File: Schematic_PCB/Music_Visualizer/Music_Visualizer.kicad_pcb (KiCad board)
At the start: 2 copper layers, 115 parts, among them J1 AudioJack2_Ground, SW1 SW_SPDT, U1 LM324, U2 LM324, U3 LM324, U4 LM324, U5 LM324, U6 LM324

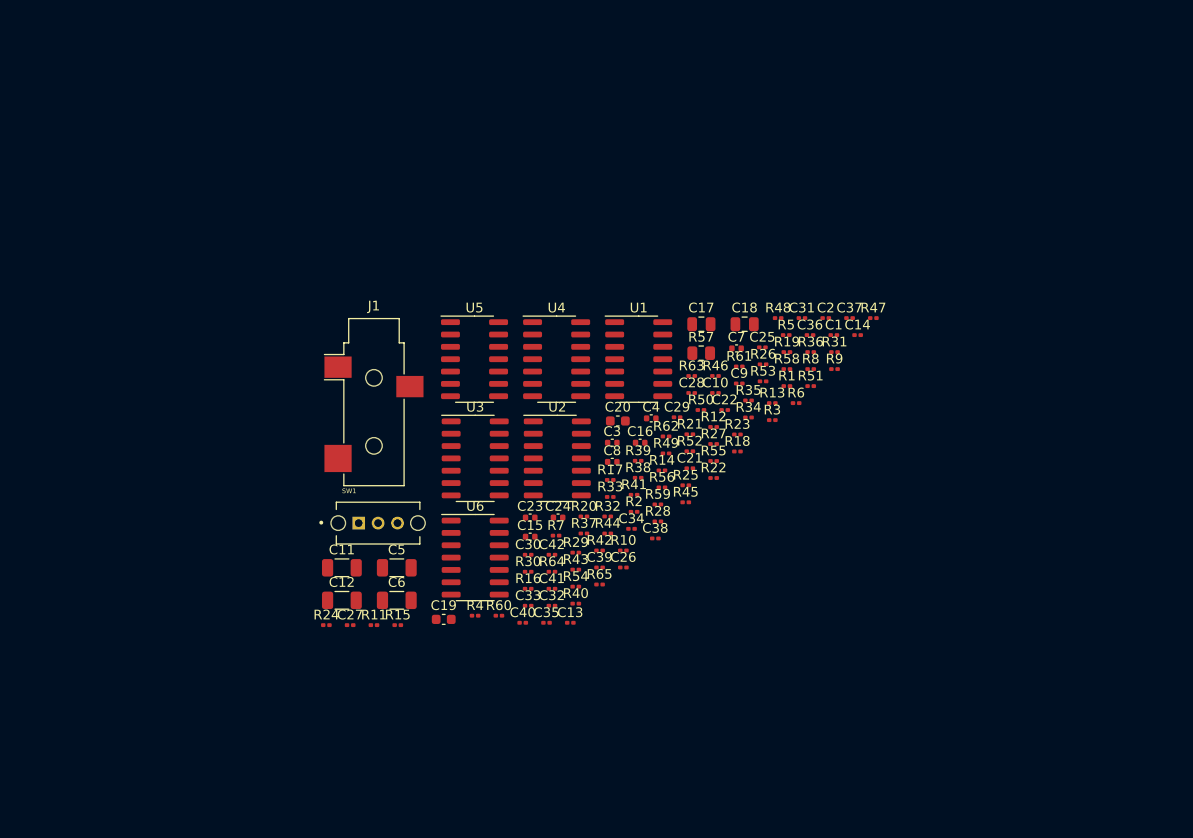
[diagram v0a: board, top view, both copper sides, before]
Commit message: Used Global labels
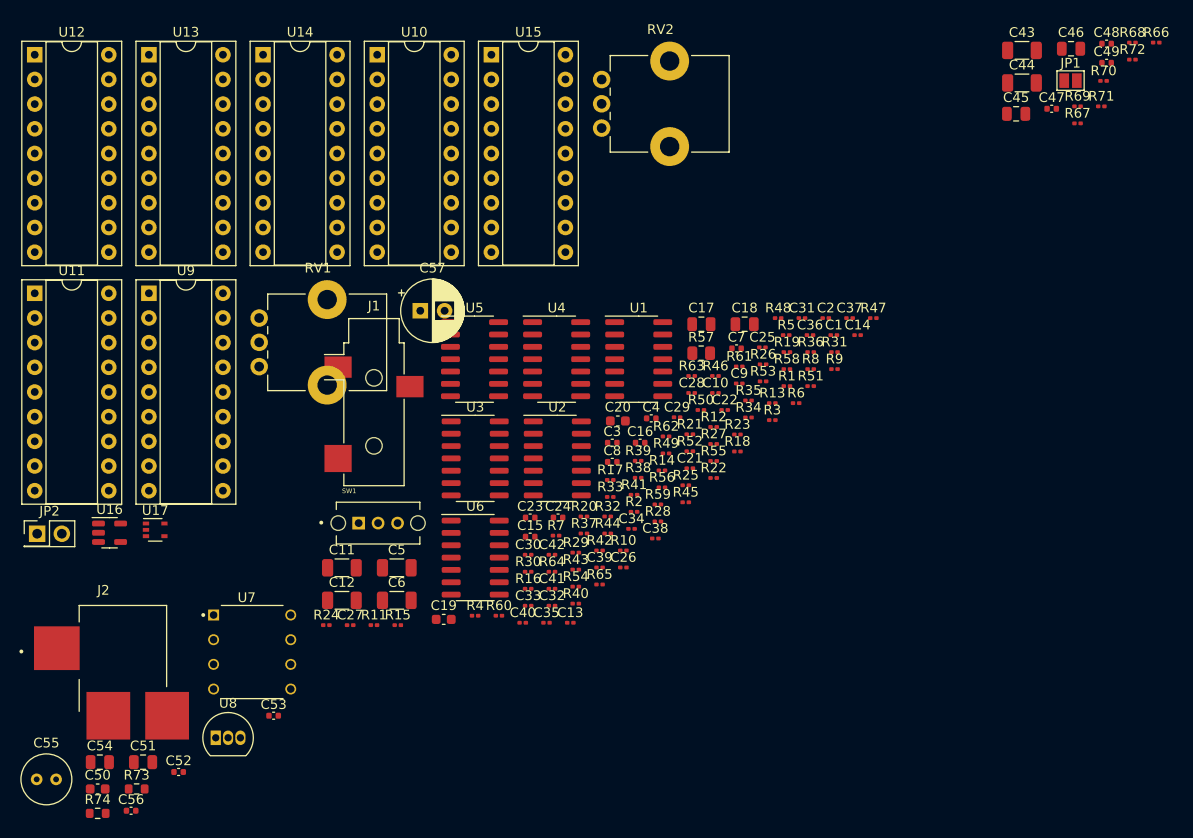
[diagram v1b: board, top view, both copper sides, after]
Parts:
- added C43: 100u, Capacitor_SMD:C_1206_3216Metric, F.Cu at (103.2, 1.18)
- added C44: 100u, Capacitor_SMD:C_1206_3216Metric, F.Cu at (103.2, 4.53)
- added C45: 10u, Capacitor_SMD:C_0805_2012Metric, F.Cu at (102.6, 7.71)
- added C46: 10u, Capacitor_SMD:C_0805_2012Metric, F.Cu at (108.2, 1.00)
- added C47: 1u, Capacitor_SMD:C_0402_1005Metric, F.Cu at (106.2, 7.18)
- added C48: 1u, Capacitor_SMD:C_0402_1005Metric, F.Cu at (111.9, 0.48)
- added C49: 1u, Capacitor_SMD:C_0402_1005Metric, F.Cu at (111.9, 2.46)
- added C50: 0.33uF, Capacitor_SMD:C_0603_1608Metric, F.Cu at (8.05, 77.2)
- added C51: 0.1uF, Capacitor_SMD:C_0805_2012Metric, F.Cu at (12.7, 74.4)
- added C52: 1u, Capacitor_SMD:C_0402_1005Metric, F.Cu at (16.4, 75.4)
- added C53: 1u, Capacitor_SMD:C_0402_1005Metric, F.Cu at (26.2, 69.7)
- added C54: 10u, Capacitor_SMD:C_0805_2012Metric, F.Cu at (8.28, 74.4)
- added C55: 100u, Capacitor_THT:C_Radial_D5.0mm_H5.0mm_P2.00mm, F.Cu at (1.77, 76.2)
- added C56: 0.002u, Capacitor_SMD:C_0402_1005Metric, F.Cu at (11.5, 79.4)
- added C57: 220u, Capacitor_THT:CP_Radial_D6.3mm_P2.50mm, F.Cu at (41.3, 28.0)
- added J2: PJ-070BH-SMT-TR, DC_Power_Jack_PJ_070BH_SMT_TR:CUI_PJ-PJ-070BH-SMT-TR, F.Cu at (10.7, 63.8)
- added JP1: SolderJumper_2_Open, Jumper:SolderJumper-2_P1.3mm_Open_Pad1.0x1.5mm, F.Cu at (108.2, 4.29)
- added JP2: Jumper_2_Open, Connector_PinHeader_2.54mm:PinHeader_2x01_P2.54mm_Vertical, F.Cu at (1.82, 50.9)
- added R66: 1k, Resistor_SMD:R_0201_0603Metric, F.Cu at (117.0, 0.38)
- added R67: 1k, Resistor_SMD:R_0201_0603Metric, F.Cu at (108.9, 8.69)
- added R68: 1k, Resistor_SMD:R_0201_0603Metric, F.Cu at (114.6, 0.38)
- added R69: 1k, Resistor_SMD:R_0201_0603Metric, F.Cu at (108.9, 6.93)
- added R70: 1k, Resistor_SMD:R_0201_0603Metric, F.Cu at (111.6, 4.32)
- added R71: 1k, Resistor_SMD:R_0201_0603Metric, F.Cu at (111.4, 6.93)
- added R72: 1k, Resistor_SMD:R_0201_0603Metric, F.Cu at (114.6, 2.12)
- added R73: 20k, Resistor_SMD:R_0603_1608Metric, F.Cu at (12.1, 77.2)
- added R74: 102k, Resistor_SMD:R_0603_1608Metric, F.Cu at (8.05, 79.7)
- added RV1: 5k_LED_Brightness_Pot, Potentiometer_THT:Potentiometer_Bourns_PTV09A-1_Single_Vertical, F.Cu at (24.7, 33.7)
- added RV2: 5k_Rhi_Adjuster, Potentiometer_THT:Potentiometer_Bourns_PTV09A-1_Single_Vertical, F.Cu at (59.9, 9.18)
- added U10: LM3915N-1, Package_DIP:DIP-18_W7.62mm_Socket, F.Cu at (36.8, 1.62)
- added U11: LM3915N-1, Package_DIP:DIP-18_W7.62mm_Socket, F.Cu at (1.57, 26.2)
- added U12: LM3915N-1, Package_DIP:DIP-18_W7.62mm_Socket, F.Cu at (1.57, 1.62)
- added U13: LM3915N-1, Package_DIP:DIP-18_W7.62mm_Socket, F.Cu at (13.3, 1.62)
- added U14: LM3915N-1, Package_DIP:DIP-18_W7.62mm_Socket, F.Cu at (25.1, 1.62)
- added U15: LM3915N-1, Package_DIP:DIP-18_W7.62mm_Socket, F.Cu at (48.6, 1.62)
- added U16: NCP161ASN350T1G, Package_TO_SOT_SMD:SOT-23-5, F.Cu at (9.28, 50.8)
- added U17: NCS333ASQ3T2G, Package_TO_SOT_SMD:SOT-353_SC-70-5, F.Cu at (14.0, 50.5)
- added U7: LT1054, LT1054_PDIP_Lin_Reg:DIP794W45P254L959H508Q8, F.Cu at (24.0, 63.1)
- added U8: MC78L05_TO92, Package_TO_SOT_THT:TO-92_Inline, F.Cu at (20.2, 71.9)
- added U9: LM3915N-1, Package_DIP:DIP-18_W7.62mm_Socket, F.Cu at (13.3, 26.2)
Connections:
- J1 pad T: /Vsig -> Net-(J1-PadT)
- R1 pad 1: /Vsig -> Vsig
- R10 pad 1: /Vsig -> Vsig
- R20 pad 1: /Vsig -> Vsig
- R29 pad 1: /Vsig -> Vsig
- R39 pad 1: /Vsig -> Vsig
- R48 pad 1: /Vsig -> Vsig
- R57 pad 1: /Vsig -> Vsig
- SW1 pad 1: unconnected-(SW1-Pad1) -> /Vsig_male
- SW1 pad 2: unconnected-(SW1-Pad2) -> Vsig
- SW1 pad 3: unconnected-(SW1-Pad3) -> Net-(J1-PadT)

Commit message: Start PCB
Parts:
- added D1: LED, LED_THT:LED_D5.0mm, F.Cu at (124.8, 35.4)
- added D10: LED, LED_THT:LED_D5.0mm, F.Cu at (87.3, 35.4)
- added D11: LED, LED_THT:LED_D5.0mm, F.Cu at (44.6, 59.2)
- added D12: LED, LED_THT:LED_D5.0mm, F.Cu at (67.1, 60.0)
- added D13: LED, LED_THT:LED_D5.0mm, F.Cu at (75.0, 52.4)
- added D14: LED, LED_THT:LED_D5.0mm, F.Cu at (90.0, 43.0)
- added D15: LED, LED_THT:LED_D5.0mm, F.Cu at (44.0, 81.9)
- added D16: LED, LED_THT:LED_D5.0mm, F.Cu at (59.6, 67.5)
- added D17: LED, LED_THT:LED_D5.0mm, F.Cu at (125.3, 27.9)
- added D18: LED, LED_THT:LED_D5.0mm, F.Cu at (36.5, 77.0)
- added D19: LED, LED_THT:LED_D5.0mm, F.Cu at (82.1, 73.5)
- added D2: LED, LED_THT:LED_D5.0mm, F.Cu at (51.5, 81.9)
- added D20: LED, LED_THT:LED_D5.0mm, F.Cu at (97.5, 50.5)
- added D21: LED, LED_THT:LED_D5.0mm, F.Cu at (90.0, 50.5)
- added D22: LED, LED_THT:LED_D5.0mm, F.Cu at (95.3, 27.9)
- added D23: LED, LED_THT:LED_D5.0mm, F.Cu at (74.0, 82.6)
- added D24: LED, LED_THT:LED_D5.0mm, F.Cu at (140.3, 20.3)
- added D25: LED, LED_THT:LED_D5.0mm, F.Cu at (82.5, 50.8)
- added D26: LED, LED_THT:LED_D5.0mm, F.Cu at (132.8, 20.3)
- added D27: LED, LED_THT:LED_D5.0mm, F.Cu at (28.6, 83.8)
- added D28: LED, LED_THT:LED_D5.0mm, F.Cu at (132.8, 27.9)
- added D29: LED, LED_THT:LED_D5.0mm, F.Cu at (117.3, 35.4)
- added D3: LED, LED_THT:LED_D5.0mm, F.Cu at (67.1, 67.5)
- added D30: LED, LED_THT:LED_D5.0mm, F.Cu at (21.1, 83.8)
- added D31: LED, LED_THT:LED_D5.0mm, F.Cu at (95.3, 20.3)
- added D32: LED, LED_THT:LED_D5.0mm, F.Cu at (52.1, 59.2)
- added D33: LED, LED_THT:LED_D5.0mm, F.Cu at (102.3, 35.4)
- added D34: LED, LED_THT:LED_D5.0mm, F.Cu at (36.5, 69.4)
- added D35: LED, LED_THT:LED_D5.0mm, F.Cu at (66.5, 75.1)
- added D36: LED, LED_THT:LED_D5.0mm, F.Cu at (36.1, 84.5)
- added D37: LED, LED_THT:LED_D5.0mm, F.Cu at (90.0, 58.1)
- added D38: LED, LED_THT:LED_D5.0mm, F.Cu at (120.0, 43.0)
- added D39: LED, LED_THT:LED_D5.0mm, F.Cu at (89.6, 65.9)
- added D4: LED, LED_THT:LED_D5.0mm, F.Cu at (67.5, 44.9)
- added D40: LED, LED_THT:LED_D5.0mm, F.Cu at (110.3, 27.9)
- added D41: LED, LED_THT:LED_D5.0mm, F.Cu at (52.1, 66.8)
- added D42: LED, LED_THT:LED_D5.0mm, F.Cu at (44.6, 66.8)
- added D43: LED, LED_THT:LED_D5.0mm, F.Cu at (59.0, 75.1)
- added D44: LED, LED_THT:LED_D5.0mm, F.Cu at (75.0, 44.9)
- added D45: LED, LED_THT:LED_D5.0mm, F.Cu at (82.1, 65.9)
- added D46: LED, LED_THT:LED_D5.0mm, F.Cu at (125.3, 20.3)
- added D47: LED, LED_THT:LED_D5.0mm, F.Cu at (60.0, 44.9)
- added D48: LED, LED_THT:LED_D5.0mm, F.Cu at (59.0, 82.6)
- added D49: LED, LED_THT:LED_D5.0mm, F.Cu at (74.6, 67.5)
- added D5: LED, LED_THT:LED_D5.0mm, F.Cu at (60.0, 52.4)
- added D50: LED, LED_THT:LED_D5.0mm, F.Cu at (82.5, 43.3)
- added D51: LED, LED_THT:LED_D5.0mm, F.Cu at (117.8, 20.3)
- added D52: LED, LED_THT:LED_D5.0mm, F.Cu at (66.5, 82.6)
- added D53: LED, LED_THT:LED_D5.0mm, F.Cu at (44.0, 74.3)
- added D54: LED, LED_THT:LED_D5.0mm, F.Cu at (97.5, 43.0)
- added D55: LED, LED_THT:LED_D5.0mm, F.Cu at (105.0, 50.5)
- added D56: LED, LED_THT:LED_D5.0mm, F.Cu at (105.0, 43.0)
- added D57: LED, LED_THT:LED_D5.0mm, F.Cu at (79.8, 28.2)
- added D58: LED, LED_THT:LED_D5.0mm, F.Cu at (87.8, 20.3)
- added D59: LED, LED_THT:LED_D5.0mm, F.Cu at (109.8, 35.4)
- added D6: LED, LED_THT:LED_D5.0mm, F.Cu at (74.0, 75.1)
- added D60: LED, LED_THT:LED_D5.0mm, F.Cu at (117.8, 27.9)
- added D61: LED, LED_THT:LED_D5.0mm, F.Cu at (74.6, 60.0)
- added D62: LED, LED_THT:LED_D5.0mm, F.Cu at (51.5, 74.3)
- added D63: LED, LED_THT:LED_D5.0mm, F.Cu at (67.5, 52.4)
- added D64: LED, LED_THT:LED_D5.0mm, F.Cu at (94.8, 35.4)
- added D65: LED, LED_THT:LED_D5.0mm, F.Cu at (97.5, 58.1)
- added D66: LED, LED_THT:LED_D5.0mm, F.Cu at (110.3, 20.3)
- added D67: LED, LED_THT:LED_D5.0mm, F.Cu at (102.8, 20.3)
- added D68: LED, LED_THT:LED_D5.0mm, F.Cu at (102.8, 27.9)
- added D69: LED, LED_THT:LED_D5.0mm, F.Cu at (82.5, 58.4)
- added D7: LED, LED_THT:LED_D5.0mm, F.Cu at (79.8, 35.7)
- added D70: LED, LED_THT:LED_D5.0mm, F.Cu at (87.8, 27.9)
- added D8: LED, LED_THT:LED_D5.0mm, F.Cu at (59.6, 60.0)
- added D9: LED, LED_THT:LED_D5.0mm, F.Cu at (112.5, 43.0)
- added R75: 680, Resistor_SMD:R_0603_1608Metric, F.Cu at (47.3, 86.9)
- added R76: 680, Resistor_SMD:R_0603_1608Metric, F.Cu at (59.4, 87.7)
- added R77: 680, Resistor_SMD:R_0603_1608Metric, F.Cu at (67.4, 87.7)
- added R78: 680, Resistor_SMD:R_0603_1608Metric, F.Cu at (71.4, 87.7)
- added R79: 680, Resistor_SMD:R_0603_1608Metric, F.Cu at (63.4, 87.7)
- added R80: 680, Resistor_SMD:R_0603_1608Metric, F.Cu at (51.4, 86.9)
- added R81: 680, Resistor_SMD:R_0603_1608Metric, F.Cu at (55.4, 87.7)
- SW1: footprint local:SW_OS102011MS2QN1 -> Slide_Switch:SW_OS102011MS2QN1
- moved C50 157.8 mm to (160.4, 36.2)
- moved C51 157.8 mm to (165.1, 33.5)
- moved C52 157.8 mm to (168.8, 34.5)
- moved C53 157.8 mm to (178.5, 28.7)
- moved C54 157.8 mm to (160.7, 33.5)
- moved C55 157.8 mm to (154.2, 35.2)
- moved C56 157.8 mm to (163.9, 38.5)
- moved J2 157.8 mm to (163.0, 22.8)
- moved R73 157.8 mm to (164.4, 36.2)
- moved R74 157.8 mm to (160.4, 38.7)
- moved U7 157.8 mm to (176.3, 22.1)
- moved U8 157.8 mm to (172.6, 30.9)
- moved C46 145.5 mm to (32.1, 125.0)
- moved C44 143.4 mm to (27.1, 126.1)
- moved R68 141.6 mm to (40.6, 121.1)
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
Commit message: Organized all subcircuits in PCB editor
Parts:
- added C58: 1u, Capacitor_SMD:C_0402_1005Metric, F.Cu at (281.9, 245.5)
- added C59: 1u, Capacitor_SMD:C_0402_1005Metric, F.Cu at (269.9, 245.5)
- moved R81 479.0 mm to (533.5, 59.2), turned to -90 degrees
- moved U15 460.1 mm to (524.5, 73.7), turned to 180 degrees
- moved JP2 437.5 mm to (549.0, 22.0)
- moved D62 432.3 mm to (482.6, 106.7), turned to 180 degrees
- moved R74 419.8 mm to (556.0, 179.2), turned to -90 degrees
- moved D63 417.4 mm to (482.6, 96.5), turned to 180 degrees
- moved D61 412.0 mm to (482.6, 116.8), turned to 180 degrees
- moved C56 411.9 mm to (551.0, 179.0), turned to -90 degrees
- moved C52 408.7 mm to (554.0, 171.0), turned to -90 degrees
- moved J2 405.5 mm to (550.8, 141.5)
- moved C55 403.0 mm to (531.0, 178.0), turned to 90 degrees
- moved R73 402.3 mm to (539.0, 183.0)
- moved D69 400.7 mm to (482.6, 35.6), turned to 180 degrees
- moved R80 399.2 mm to (449.6, 59.2), turned to -90 degrees
- moved C53 397.8 mm to (550.0, 171.0), turned to -90 degrees
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
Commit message: Got 3D models for all parts, corrected signal voltage to each driver and made outline of PCB
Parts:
- added D71: LED, LED_THT:LED_D5.0mm, F.Cu at (431.2, 207.4)
- added R82: 330, Resistor_SMD:R_0603_1608Metric, F.Cu at (423.7, 177.0)
- added SW2: SW_SPST, PW_On_Off_Switch:E-SWITCH_RR511D1121, F.Cu at (416.2, 162.4)
- J2: value PJ-070BH-SMT-TR -> PJ-079BH; footprint DC_Power_Jack_PJ_070BH_SMT_TR:CUI_PJ-PJ-070BH-SMT-TR -> DC_Power_Jack_PJ_070BH:CUI_PJ-079BH
- RV1: value 5k_LED_Brightness_Pot -> 10k_LED_Brightness_Pot; footprint Potentiometer_THT:Potentiometer_Bourns_PTV09A-1_Single_Vertical -> PTV111_Horizontal:TRIM_PTV111-1415A-B203
- moved JP2 211.2 mm to (408.7, 179.9)
- moved C50 152.5 mm to (386.1, 181.7)
- moved C51 152.5 mm to (367.1, 183.9)
- moved U8 152.5 mm to (377.1, 183.9)
- moved C52 134.8 mm to (420.9, 192.9)
- moved C53 134.8 mm to (416.9, 192.9)
- moved C54 134.8 mm to (390.9, 194.9)
- moved C55 134.8 mm to (397.9, 199.9)
- moved C56 134.8 mm to (417.9, 200.9)
- moved R73 134.8 mm to (405.9, 204.9)
- moved R74 134.8 mm to (422.9, 201.1)
- moved U7 134.8 mm to (408.9, 195.9)
- moved J2 121.5 mm to (439.9, 191.2), turned to 180 degrees
- moved R81 119.4 mm to (416.5, 83.2)
- moved U15 119.4 mm to (407.5, 97.6)
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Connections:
- net Net-(J1-PadT) renamed /Vsig_female
- C59 pad 1: Net-(RV2-Pad1) -> Net-(C59-Pad1)
- J2 pad 1: +9V -> /Power/Power
- RV2 pad 1: Net-(RV2-Pad1) -> GND
- RV2 pad 3: GND -> Net-(C59-Pad1)
- U10 pad 5: VSubBass -> VBass
- U11 pad 5: VSubBass -> VLowerMidrange
- U12 pad 5: VSubBass -> VMidrange
- U13 pad 5: VSubBass -> VUpperMidrange
- U14 pad 5: VSubBass -> VPresence
- U15 pad 5: VSubBass -> VBrilliance
- U16 pad 5: Net-(RV2-Pad1) -> Net-(C59-Pad1)
- U6 pad 10: unconnected-(U6-Pad10) -> Net-(U6-Pad10)
- U6 pad 12: unconnected-(U6-Pad12) -> Net-(U6-Pad12)
- U6 pad 13: unconnected-(U6-Pad13) -> Net-(U6-Pad13)
- U6 pad 14: unconnected-(U6-Pad14) -> Net-(U6-Pad12)
- U6 pad 5: unconnected-(U6-Pad5) -> Net-(U6-Pad5)
- U6 pad 6: unconnected-(U6-Pad6) -> Net-(U6-Pad13)
- U6 pad 7: unconnected-(U6-Pad7) -> Net-(U6-Pad5)
- U6 pad 8: unconnected-(U6-Pad8) -> Net-(U6-Pad10)
- U6 pad 9: unconnected-(U6-Pad9) -> Net-(U6-Pad13)
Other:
- board outline added: 392.5 x 200 mm
- board text added: "Bass [60Hz:250Hz]"
- board text added: "Brilliance [6kHz:20kHz]"
- board text added: "Lower-Midrange [250Hz:500Hz]"
- board text added: "Midrange [500Hz:2kHz]"
- board text added: "Presence [4kHz:6kHz]"
- board text added: "Sub-Bass [20Hz:60Hz]"
- board text added: "Upperr-Midrange [2kHz:4kHz]"

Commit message: Formated LEDs, LED drivers and filters in PCB editor
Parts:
- moved U6 114.5 mm to (296.0, 125.0)
- moved R81 70.5 mm to (346.0, 84.0), turned to 90 degrees
- moved U15 67.5 mm to (340.0, 100.0)
- moved C49 65.9 mm to (346.0, 91.0), turned to 90 degrees
- moved R72 63.4 mm to (351.0, 90.0)
- moved C48 61.4 mm to (306.0, 91.0), turned to 90 degrees
- moved R80 60.7 mm to (306.0, 84.0), turned to 90 degrees
- moved R71 59.4 mm to (311.0, 90.0)
- moved D61 58.7 mm to (325.0, 140.0)
- moved D70 58.7 mm to (325.0, 50.0)
- moved D62 58.7 mm to (325.0, 130.0)
- moved D69 58.7 mm to (325.0, 60.0)
- moved D63 58.7 mm to (325.0, 120.0)
- moved D68 58.7 mm to (325.0, 70.0)
- moved D64 58.7 mm to (325.0, 110.0)
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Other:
- board text added: "Upper-Midrange [2kHz:4kHz]"
- board text removed: "Upperr-Midrange [2kHz:4kHz]"

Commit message: Labelled necessary subcircuits in the PCB Editor
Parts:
- moved D71 98.4 mm to (337.0, 179.0)
- moved C50 86.1 mm to (335.5, 112.0), turned to 0 degrees
- moved C57 79.2 mm to (349.5, 148.0)
- moved JP2 77.6 mm to (338.0, 148.0)
- moved U8 77.2 mm to (337.0, 118.0), turned to 180 degrees
- moved R74 75.5 mm to (356.1, 166.1)
- moved J2 75.1 mm to (372.2, 158.8)
- moved C56 74.6 mm to (352.1, 166.0)
- moved C52 73.7 mm to (356.1, 158.0)
- moved C53 73.7 mm to (352.1, 158.0)
- moved U7 72.9 mm to (345.0, 161.0)
- moved C55 71.9 mm to (335.1, 165.0)
- moved R82 71.7 mm to (356.5, 152.0)
- moved R73 70.7 mm to (345.1, 169.1)
- moved C54 69.3 mm to (331.1, 159.9)
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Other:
- board size 392.5 x 200 mm -> 320 x 175.1 mm
- board text added: "Jack Source"
- board text added: "LED Brightness Control"
- board text added: "Plug Source"
- board text added: "Power"
- board text added: "Volume Range Control"

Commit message: Both parts ar PVT09A 5K ohms, corrected footprint terminal labels
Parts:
- RV1: footprint PTV111_Horizontal:TRIM_PTV111-1415A-B203 -> PTV09A_Pot_Vertical:PTV09
- RV2: footprint Potentiometer_THT:Potentiometer_Bourns_PTV09A-1_Single_Vertical -> PTV09A_Pot_Vertical:PTV09
- moved RV2 13.4 mm to (268.0, 180.2), turned to 0 degrees
- moved RV1 8.15 mm to (187.0, 180.2)
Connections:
- RV1 pad 1: unconnected-(RV1-Pad1) -> GND
- RV1 pad 3: GND -> unconnected-(RV1-Pad3)
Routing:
- net +9V: track 0.00 -> 630.0 mm
- net Mode: track 0.00 -> 264.2 mm
- net LED_Brightness_Control: track 0.00 -> 80.6 mm, vias 0 -> 4
- net Net-(D21-Pad1): track 0.00 -> 46.2 mm
- net Net-(D11-Pad1): track 0.00 -> 46.2 mm
- net Net-(D1-Pad1): track 0.00 -> 46.2 mm
- net Net-(D30-Pad1): track 0.00 -> 35.7 mm
- net Net-(D40-Pad1): track 0.00 -> 35.1 mm
- net Net-(D50-Pad1): track 0.00 -> 33.9 mm
- net Net-(D20-Pad1): track 0.00 -> 33.9 mm
- net Net-(D10-Pad1): track 0.00 -> 33.3 mm
- net Net-(D32-Pad1): track 0.00 -> 33.1 mm
- net Net-(D22-Pad1): track 0.00 -> 33.1 mm
- net Net-(D2-Pad1): track 0.00 -> 33.1 mm
- net Net-(D12-Pad1): track 0.00 -> 33.1 mm
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- added copper zone on B.Cu, net GND

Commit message: Fully connected LEDs and driver ICs to 9V
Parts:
- moved C50 10.2 mm to (337.5, 122.0)
- moved C51 10.2 mm to (337.9, 135.0)
- moved U8 10.2 mm to (339.0, 128.0)
- moved R75 9.00 mm to (106.0, 75.0)
- moved R76 9.00 mm to (146.0, 75.0)
- moved R77 9.00 mm to (186.0, 75.0)
- moved R78 9.00 mm to (226.0, 75.0)
- moved R79 9.00 mm to (266.0, 75.0)
- moved R80 9.00 mm to (306.0, 75.0)
- moved R81 9.00 mm to (346.0, 75.0)
- moved C45 1.00 mm to (186.0, 91.0)
- moved C46 1.00 mm to (226.0, 91.0)
- moved C48 1.00 mm to (306.0, 90.0)
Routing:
- net +9V: track 630.0 -> 1014.8 mm
- net LED_Brightness_Control: track 80.6 -> 243.0 mm, vias 4 -> 12
- net GND: track 0.00 -> 97.8 mm
- net Net-(D61-Pad1): track 0.00 -> 46.2 mm
- net Net-(D51-Pad1): track 0.00 -> 46.2 mm
- net Net-(D41-Pad1): track 0.00 -> 46.2 mm
- net Net-(D31-Pad1): track 0.00 -> 46.2 mm
- net Net-(D70-Pad1): track 0.00 -> 33.9 mm
- net Net-(D60-Pad1): track 0.00 -> 33.9 mm
- net Net-(D62-Pad1): track 0.00 -> 33.1 mm
- net Net-(D52-Pad1): track 0.00 -> 33.1 mm
- net Net-(D42-Pad1): track 0.00 -> 33.1 mm
- net Net-(D43-Pad1): track 0.00 -> 26.7 mm
- net Net-(D63-Pad1): track 0.00 -> 26.7 mm
- net Net-(D53-Pad1): track 0.00 -> 26.7 mm
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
